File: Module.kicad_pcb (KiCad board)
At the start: 6 copper layers, 30 x 41.8 mm, 134 parts

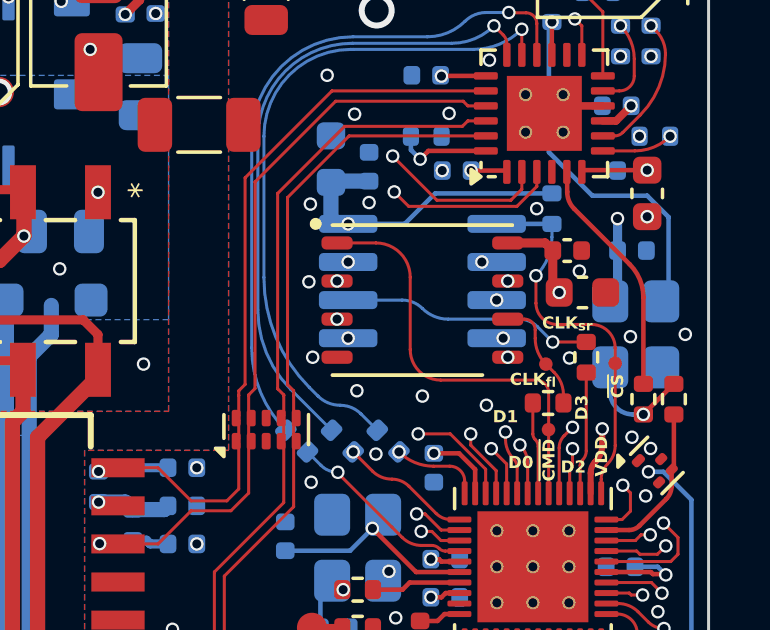
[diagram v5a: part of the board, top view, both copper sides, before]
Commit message: fixed Flash and PSRAM to MCU pinout mapping added pull-up to Flash CS pin
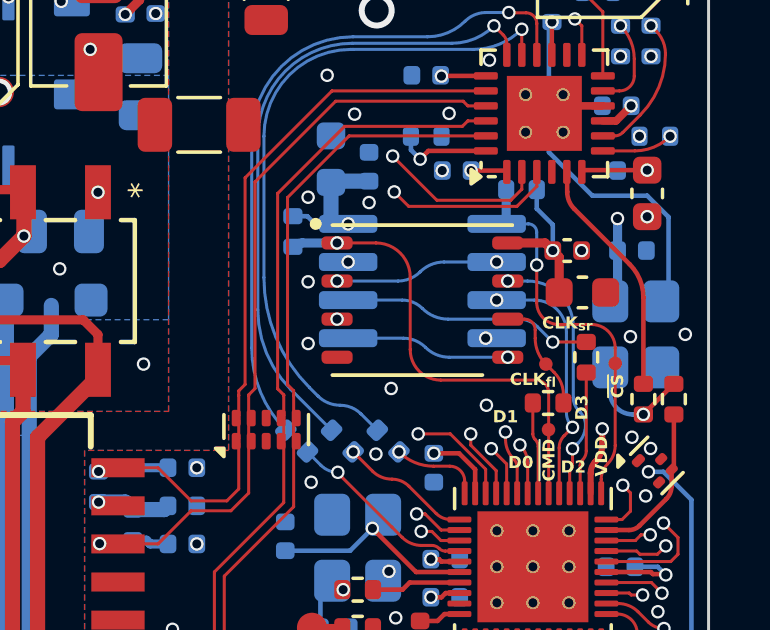
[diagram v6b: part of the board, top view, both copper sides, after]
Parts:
- added 2R39: 10K, Resistor_SMD:R_0402_1005Metric, B.Cu at (1.14, -18.8)
- moved 2R20 1.20 mm to (8.76, -20.2), turned to 180 degrees
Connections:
- 1U4 pad 28: /MCU/SD_D2 -> /MCU/SD_D3
- 1U4 pad 29: /MCU/SD_D3 -> /MCU/SD_D2
- 1U4 pad 32: /MCU/SD_D0 -> /MCU/SD_D1
- 1U4 pad 33: /MCU/SD_D1 -> /MCU/SD_D0
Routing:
- net /MCU/SD_D1: track 17.2 -> 13.8 mm
- net /MCU/VDD_SDIO: track 29.5 -> 26.5 mm
- net /MCU/SD_CMD: track 14.2 -> 15.7 mm, vias 0 -> 1
- net /MCU/SD_D2: track 13.2 -> 14.0 mm
- net /MCU/SRAM_CS: track 13.0 -> 13.6 mm
- net /MCU/SD_D0: track 10.2 -> 10.1 mm, vias 3 -> 2
- net GND: vias 51 -> 48

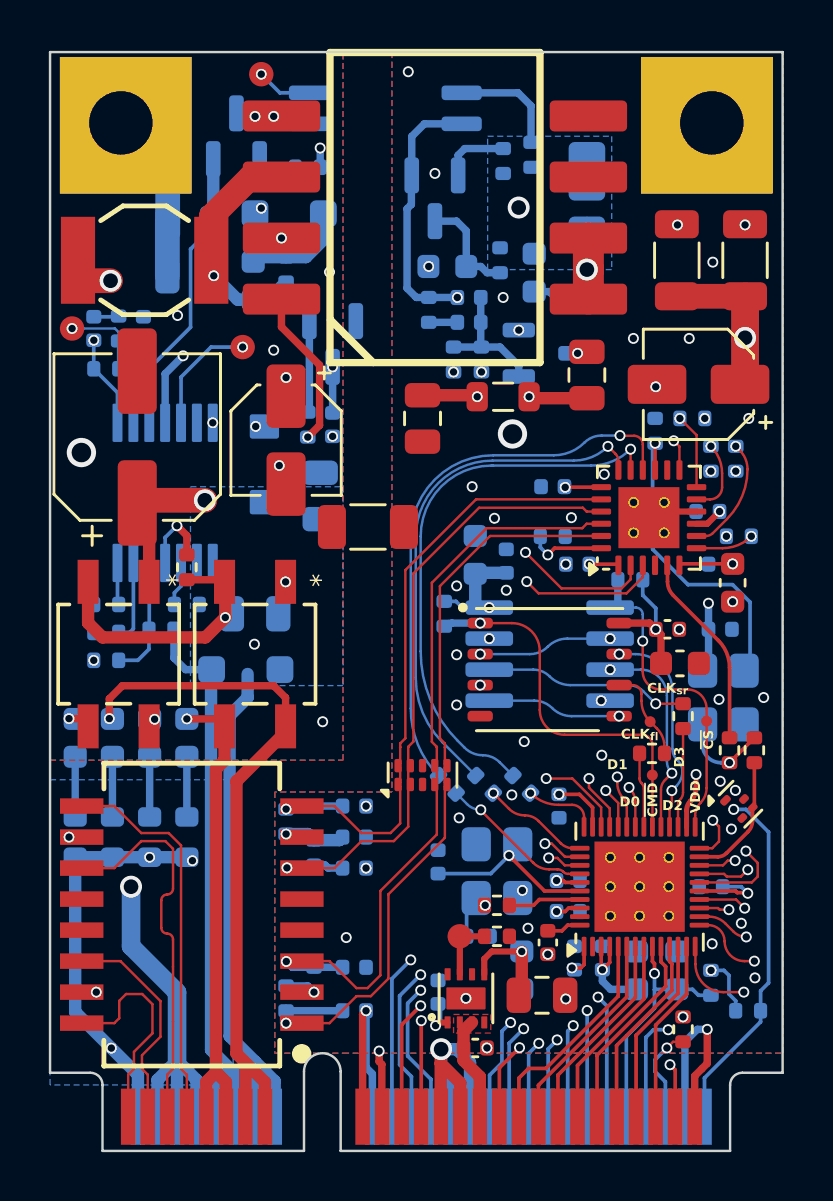
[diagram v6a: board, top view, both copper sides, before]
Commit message: small, cosmetic fixes added project url to front silkscreen
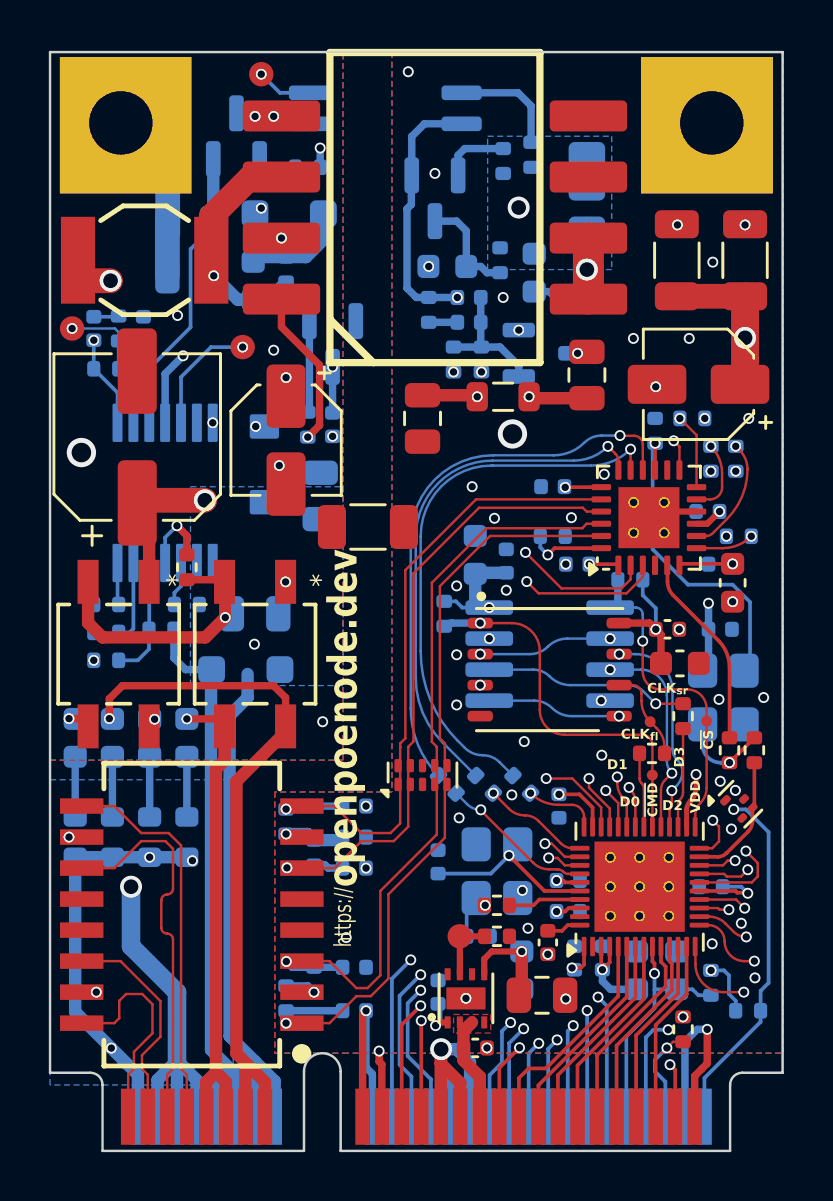
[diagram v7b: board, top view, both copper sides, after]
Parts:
- moved G*** 0.30 mm to (-2.80, -15.5)
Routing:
- net GNDPWR: vias 11 -> 10
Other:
- board text added: "https://"
- board text added: "openpoenode.dev"
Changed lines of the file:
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@@
 		)
 		(fp_circle
-			(center -3.556 -2.54)
-			(end -3.456 -2.54)
+			(center -2.8 -3)
+			(end -2.7 -3)
 			(stroke
 				(width 0.2)
@@
 		(tags "capacitor")
 		(property "Reference" "2C10"
-			(at 2.312 0.003 0)
+			(at 0.012 -0.997 0)
 			(layer "User.6")
 			(effects
@@
 		(tags "resistor")
 		(property "Reference" "2R19"
-			(at 2.312 -0.029 0)
+			(at 0.012 -1.029 0)
 			(layer "User.6")
 			(effects
@@
 		(tags "resistor")
 		(property "Reference" "2R20"
-			(at -2.322 0.009 0)
+			(at -0.137 1.007 0)
 			(layer "User.6")
 			(effects
@@
 		(tags "resistor")
 		(property "Reference" "2R14"
-			(at 0.017 -1.199 90)
+			(at -0.357 -0.045 90)
 			(layer "User.6")
 			(effects
@@
 		(tags "capacitor")
 		(property "Reference" "2C14"
-			(at -0.004 1.728 0)
+			(at -0.504 1.428 0)
 			(layer "User.6")
 			(effects
@@
 	(footprint "LOGO"
 		(layer "B.Cu")
-		(at -2.5 -15.5 90)
+		(at -2.8 -15.5 90)
 		(property "Reference" "G***"
 			(at 0 0 90)
@@
 		(tags "capacitor")
 		(property "Reference" "2C9"
-			(at -2.303 -0.045 270)
+			(at -0.057 -1.029 270)
 			(layer "User.6")
 			(effects
@@
 		(tags "SOT TO_SOT_SMD")
 		(property "Reference" "2D4"
-			(at 0 2.4 90)
-			(layer "B.SilkS")
+			(at -0.255 -0.029 90)
+			(layer "User.6")
 			(effects
 				(font
-					(size 1 1)
+					(size 0.6 0.6)
 					(thickness 0.15)
 				)
@@
 		)
 	)
+	(gr_text "https://"
+		(at -3 -7.6 90)
+		(layer "F.SilkS")
+		(effects
+			(font
+				(size 0.7 0.5)
+				(thickness 0.1)
+			)
+			(justify right)
+		)
+	)
 	(gr_text "CLK_{fl}"
 		(at 9.144 -13.8684 0)
@@
 		)
 	)
+	(gr_text "openpoenode.dev"
+		(at -3 -7.6 90)
+		(layer "F.SilkS")
+		(effects
+			(font
+				(size 1.2 1)
+				(thickness 0.2)
+				(bold yes)
+			)
+			(justify left)
+		)
+	)
 	(gr_text "~{CS}"
 		(at 11.9634 -14.0462 90)
@@
 	)
 	(via
-		(at -3.556 -32.7914)
-		(size 0.45)
-		(drill 0.3)
-		(layers "F.Cu" "B.Cu")
-		(free yes)
-		(net 2)
-	)
-	(via
